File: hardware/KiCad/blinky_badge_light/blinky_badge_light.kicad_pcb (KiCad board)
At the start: 4 copper layers, 108.6 x 87.7 mm, 121 parts, among them Q1 N-Channel MOSFET, Q2 Q_PMOS_GSD, Q3 N-Channel MOSFET, SW1 TS-1187A-B-A-B, U1 ESP32-S3-WROOM-1, U2 TP4056, U3 AP2112K-3.3, U4 MT3608, U5 CP2102N-Axx-xQFN24, U6 SN74LVC1T45DBV

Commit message: change reverse battery protection circuit so diode goes to ground
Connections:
- D28 pad 1: BAT- -> BAT+
- Q1 pad 1: BAT- -> BAT+
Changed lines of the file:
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@@
 			(layers "B.Cu" "B.Mask" "B.Paste")
 			(roundrect_rratio 0.25)
-			(net 59 "BAT-")
+			(net 1 "BAT+")
 			(pinfunction "K")
 			(pintype "passive")
@@
 			(size 1.25 0.7)
 			(layers "B.Cu" "B.Mask" "B.Paste")
-			(net 59 "BAT-")
+			(net 1 "BAT+")
 			(pinfunction "G")
 			(pintype "input")

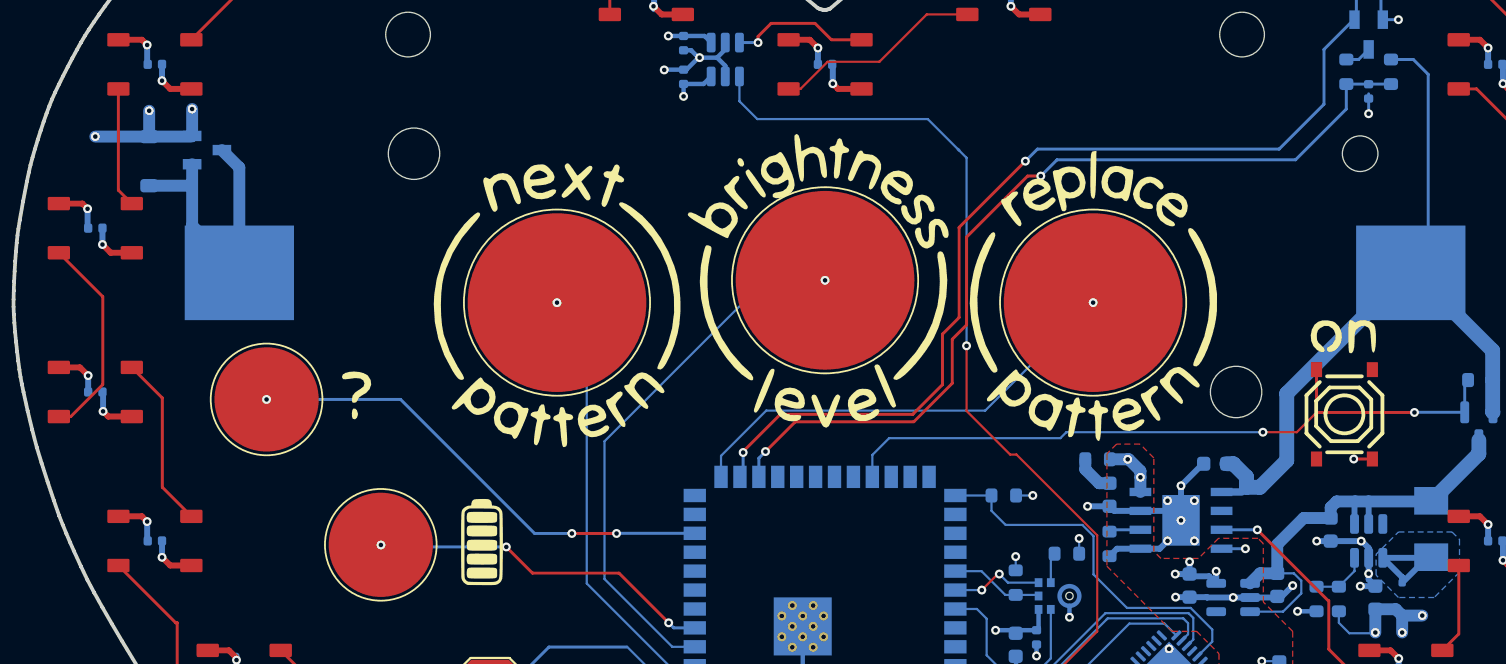
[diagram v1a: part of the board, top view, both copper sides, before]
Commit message: update battery protection circuit and draw routes
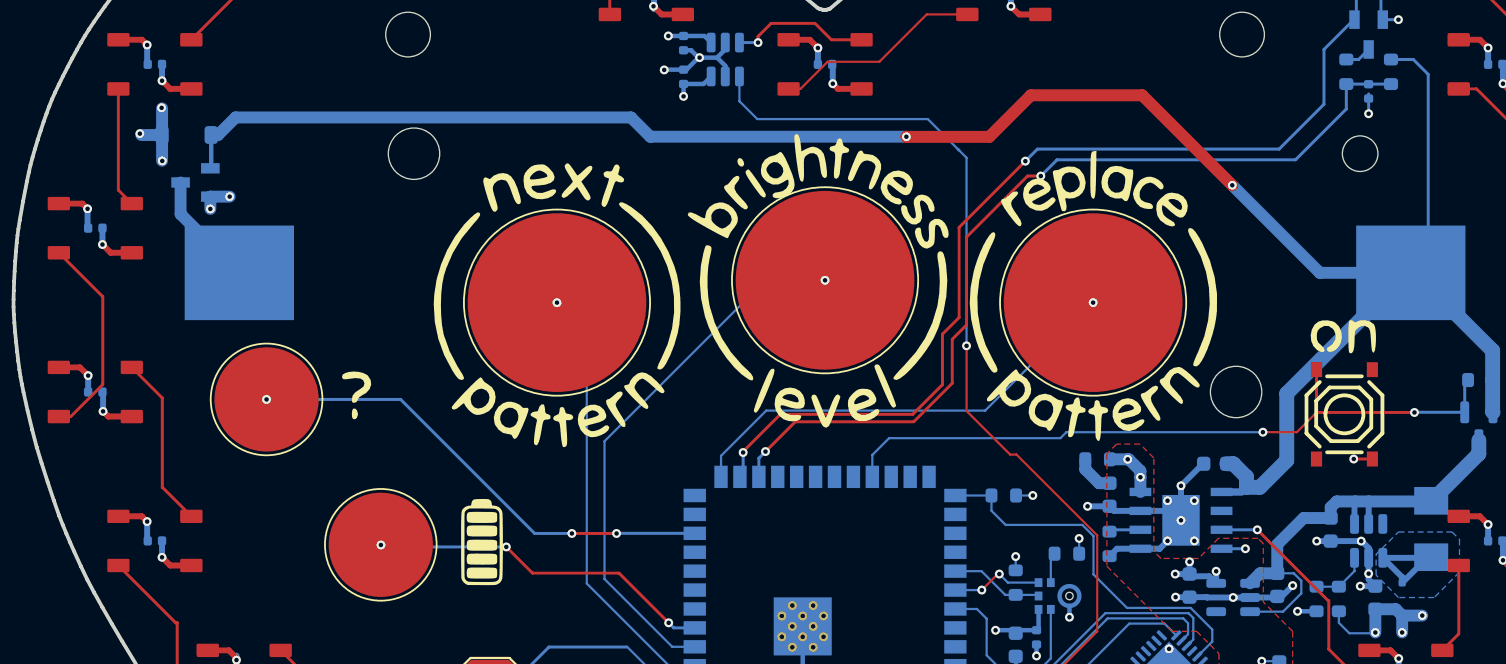
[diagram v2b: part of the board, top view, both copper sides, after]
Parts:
- R13, R18, R19: value 100kΩ -> 10kΩ
- moved D28 3.07 mm to (107.1, 71.7), turned to 180 degrees
- moved Q1 2.31 mm to (107.7, 74.9), turned to 0 degrees
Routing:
- net BAT+: track 52.0 -> 141.9 mm, vias 0 -> 2
- net BAT-: track 20.1 -> 7.70 mm
- net GND: track 179.1 -> 176.3 mm, vias 68 -> 70
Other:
- board text removed: "Battery Monitoring Circuit"
- board text removed: "Q1: is the thickness of the route from R13 to BAT+ ok or should it be thicker?"
- board text removed: "Q2: should these two grounds be the same since they're adjacent?"
- board text removed: "Q3: is it ok that the battery monitoring circuit is so far away from the ESP32?"
- board text removed: "Q4: originally BAT- had a lot of thick connections to GND. Is what I have done here enough?"
- board text removed: "Q5: this routing from battery monitoring to ESP32 is messy but not sure how to improve it.. had to do cross-over also.. open to suggestions"
- board text removed: "Q6: when I do a crossover in routing is it better to make it longer or shorter (did both types here..)"
- board text removed: "Q7a: is this pad too close to BAT -"
- board text removed: "Q7b: is this pad too close to these assorted components?"
- board text removed: "Q8: are the pads supposed to have exposed metal like the boards I got? (I'm just using the detault footprint..)"
- board text removed: "Reverse Polarity Protection"

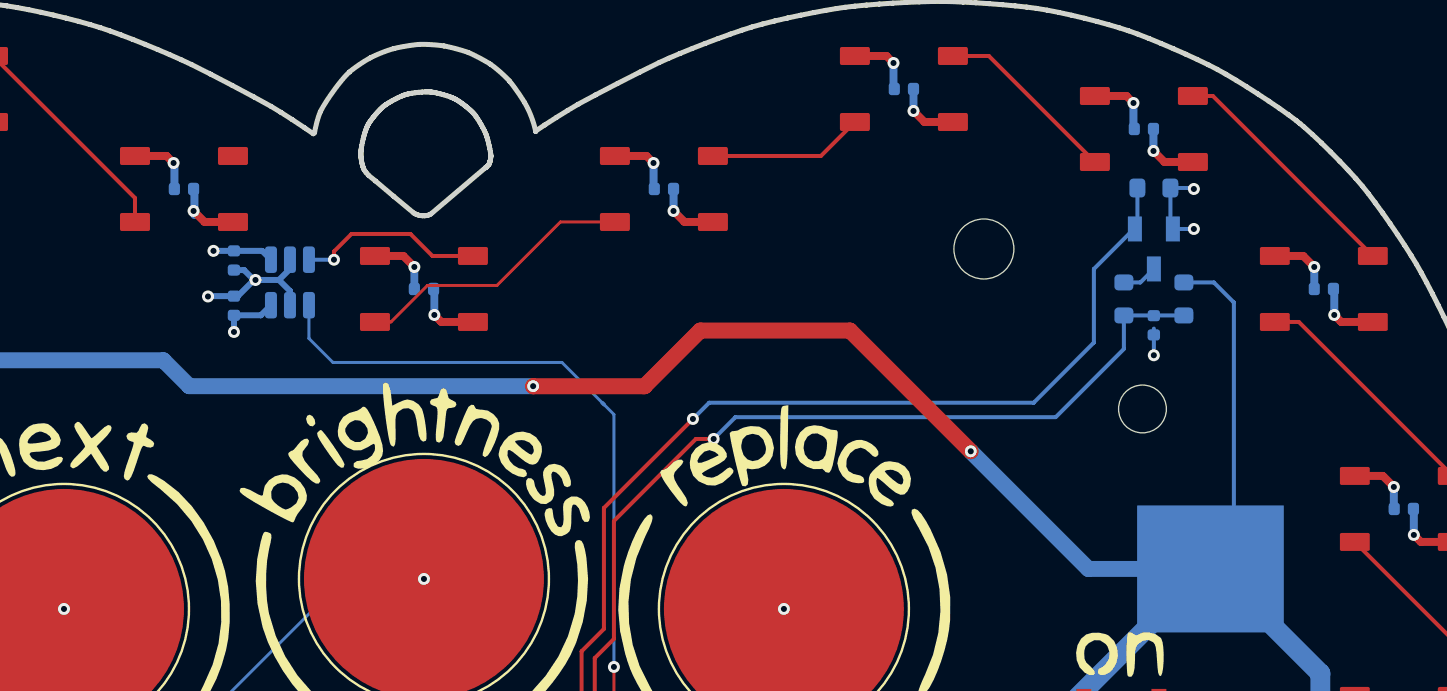
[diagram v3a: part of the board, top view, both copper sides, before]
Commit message: added new transistor and resistor to battery monitoring circuit, adjusted two leds/capacitors position slightly
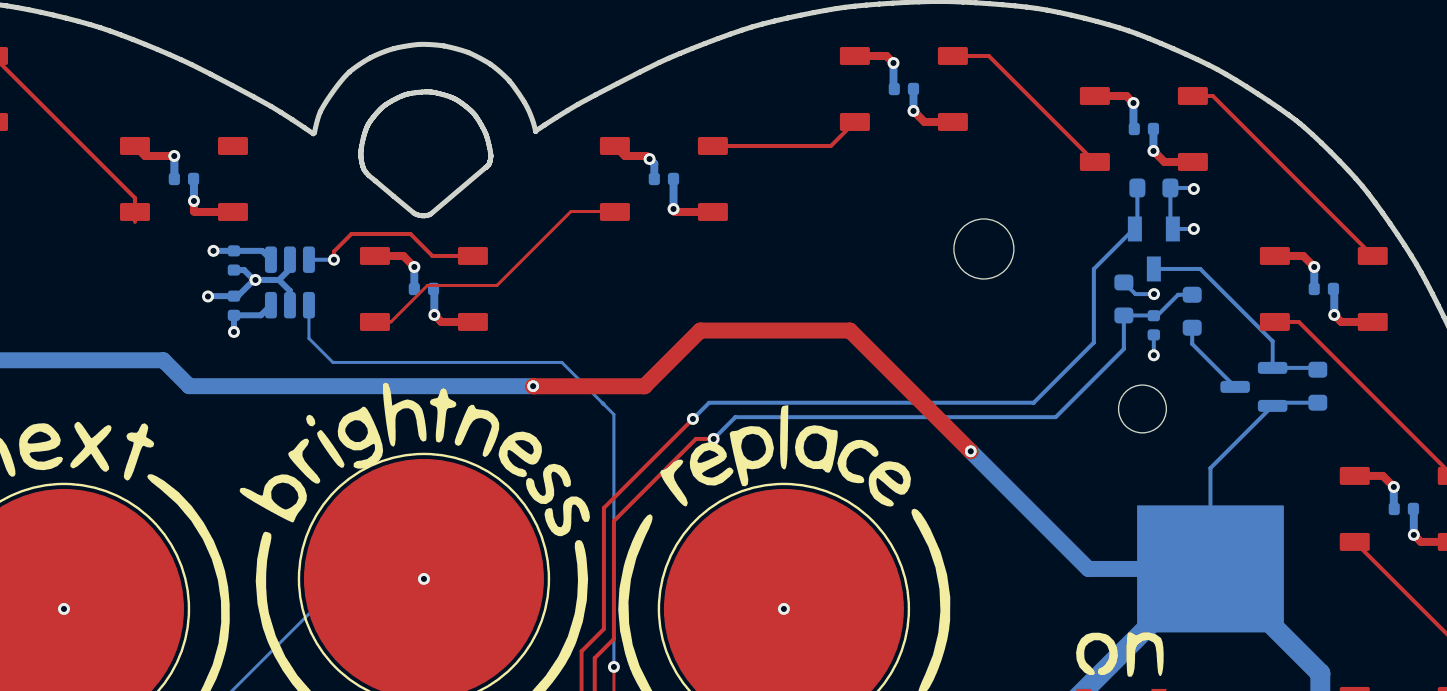
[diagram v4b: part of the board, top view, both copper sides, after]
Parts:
- added Q4: Q_PMOS_GSD, Package_TO_SOT_SMD:SOT-23, B.Cu at (191.5, 71.9)
- added R20: 100kΩ, Resistor_SMD:R_0603_1608Metric, B.Cu at (194.7, 71.9)
- R13, R18, R19: value 10kΩ -> 100kΩ
- moved G*** 4.80 mm to (124.0, 82.7)
- moved G*** 4.57 mm to (175.6, 82.1)
- moved R13 0.74 mm to (188.4, 68.1), turned to -90 degrees
- moved C2 0.50 mm to (162.0, 61.5)
- moved C24 0.50 mm to (138.0, 61.5)
- moved D2 0.50 mm to (162.0, 61.5)
- moved D24 0.50 mm to (138.0, 61.5)
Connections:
- R13 pad 2: BAT+ -> Net-(Q4-D)
- R18 pad 2: Net-(Q3-D) -> GND
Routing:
- net Net-(Q3-D): track 1.78 -> 11.1 mm
- net BAT+: track 141.9 -> 137.0 mm
- net Net-(Q4-D): track 0.00 -> 3.85 mm
- net GND: track 176.3 -> 177.9 mm, vias 70 -> 71
- net ESP32 Battery Monitoring: track 60.3 -> 61.1 mm

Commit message: changed resistors on battery monitoring (back) to 10k
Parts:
- R13, R18, R19, R20: value 100kΩ -> 10kΩ
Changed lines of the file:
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@@
 			)
 		)
-		(property "Value" "100kΩ"
+		(property "Value" "10kΩ"
 			(at 0 -1.43 90)
 			(layer "B.Fab")
@@
 			)
 		)
-		(property "Datasheet" "https://jlcpcb.com/api/file/downloadByFileSystemAccessId/8579706350726930432"
+		(property "Datasheet" "https://jlcpcb.com/api/file/downloadByFileSystemAccessId/8579706381320323072"
 			(at 0 0 270)
 			(unlocked yes)
@@
 			)
 		)
-		(property "JLCPCB Part #" "C25803"
+		(property "JLCPCB Part #" "C25804"
 			(at 0 0 270)
 			(unlocked yes)
@@
 			)
 		)
-		(property "Value" "100kΩ"
+		(property "Value" "10kΩ"
 			(at 0 -1.43 90)
 			(layer "B.Fab")
@@
 			)
 		)
-		(property "Datasheet" "https://jlcpcb.com/api/file/downloadByFileSystemAccessId/8579706350726930432"
+		(property "Datasheet" "https://jlcpcb.com/api/file/downloadByFileSystemAccessId/8579706381320323072"
 			(at 0 0 270)
 			(unlocked yes)
@@
 			)
 		)
-		(property "JLCPCB Part #" "C25803"
+		(property "JLCPCB Part #" "C25804"
 			(at 0 0 270)
 			(unlocked yes)
@@
 			)
 		)
-		(property "Value" "100kΩ"
+		(property "Value" "10kΩ"
 			(at 0 -1.43 0)
 			(layer "B.Fab")
@@
 			)
 		)
-		(property "Datasheet" "https://jlcpcb.com/api/file/downloadByFileSystemAccessId/8579706350726930432"
+		(property "Datasheet" "https://jlcpcb.com/api/file/downloadByFileSystemAccessId/8579706381320323072"
 			(at 0 0 0)
 			(unlocked yes)
@@
 			)
 		)
-		(property "JLCPCB Part #" "C25803"
+		(property "JLCPCB Part #" "C25804"
 			(at 0 0 0)
 			(unlocked yes)
@@
 			)
 		)
-		(property "Value" "100kΩ"
+		(property "Value" "10kΩ"
 			(at 0 -1.43 90)
 			(layer "B.Fab")
@@
 			)
 		)
-		(property "Datasheet" "https://jlcpcb.com/api/file/downloadByFileSystemAccessId/8579706350726930432"
+		(property "Datasheet" "https://jlcpcb.com/api/file/downloadByFileSystemAccessId/8579706381320323072"
 			(at 0 0 90)
 			(unlocked yes)
@@
 			)
 		)
-		(property "JLCPCB Part #" "C25803"
+		(property "JLCPCB Part #" "C25804"
 			(at 0 0 90)
 			(unlocked yes)

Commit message: change charging prog resistor to 2k to keep things cooler
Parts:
- R4: value 1.2kΩ -> 2kΩ
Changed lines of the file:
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@@
 			)
 		)
-		(property "Value" "1.2kΩ"
+		(property "Value" "2kΩ"
 			(at 0 -1.43 90)
 			(layer "B.Fab")
@@
 			)
 		)
-		(property "Datasheet" "https://jlcpcb.com/api/file/downloadByFileSystemAccessId/8579706389601501184"
+		(property "Datasheet" "https://jlcpcb.com/api/file/downloadByFileSystemAccessId/8579706189568917504"
 			(at 0 0 90)
 			(unlocked yes)
@@
 			)
 		)
-		(property "JLCPCB Part #" "C22764"
+		(property "JLCPCB Part #" "C22975"
 			(at 0 0 270)
 			(unlocked yes)

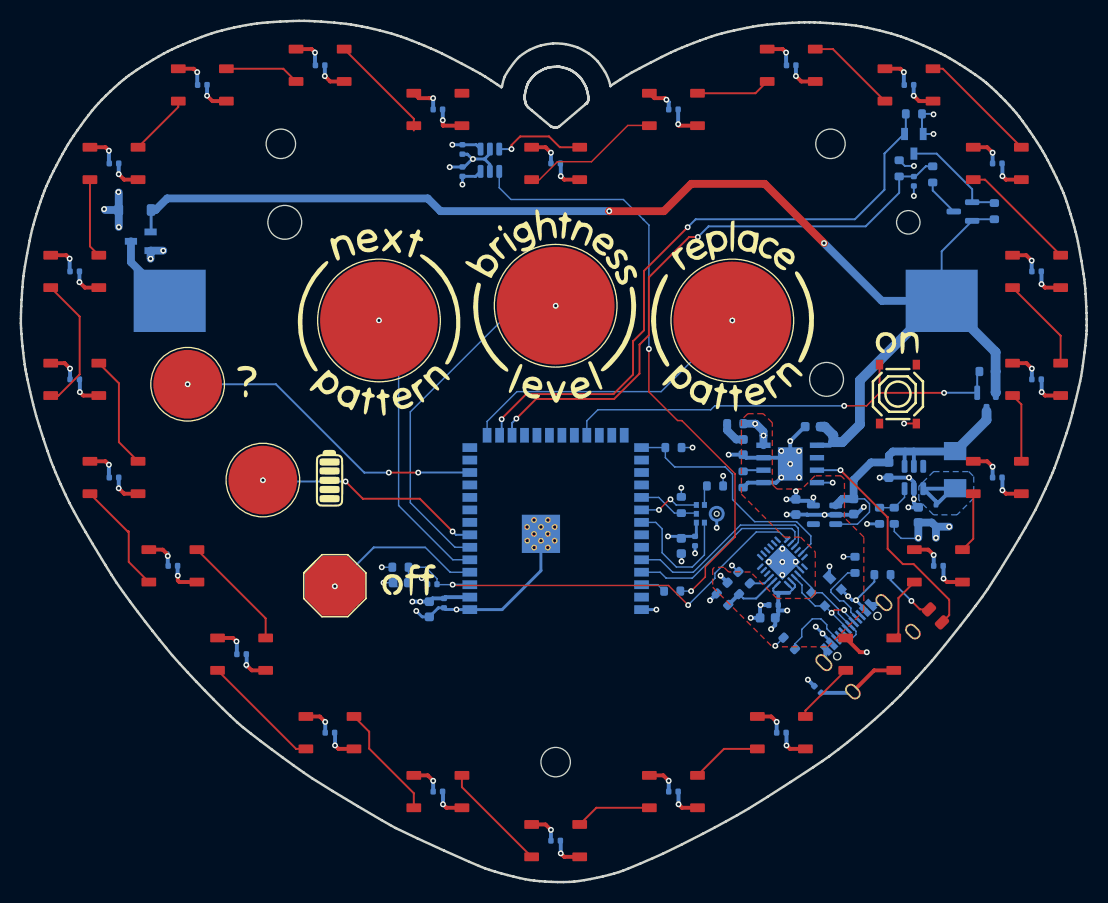
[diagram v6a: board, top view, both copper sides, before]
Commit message: slight adjusting of led positions to make things fit more nicely under the front cover
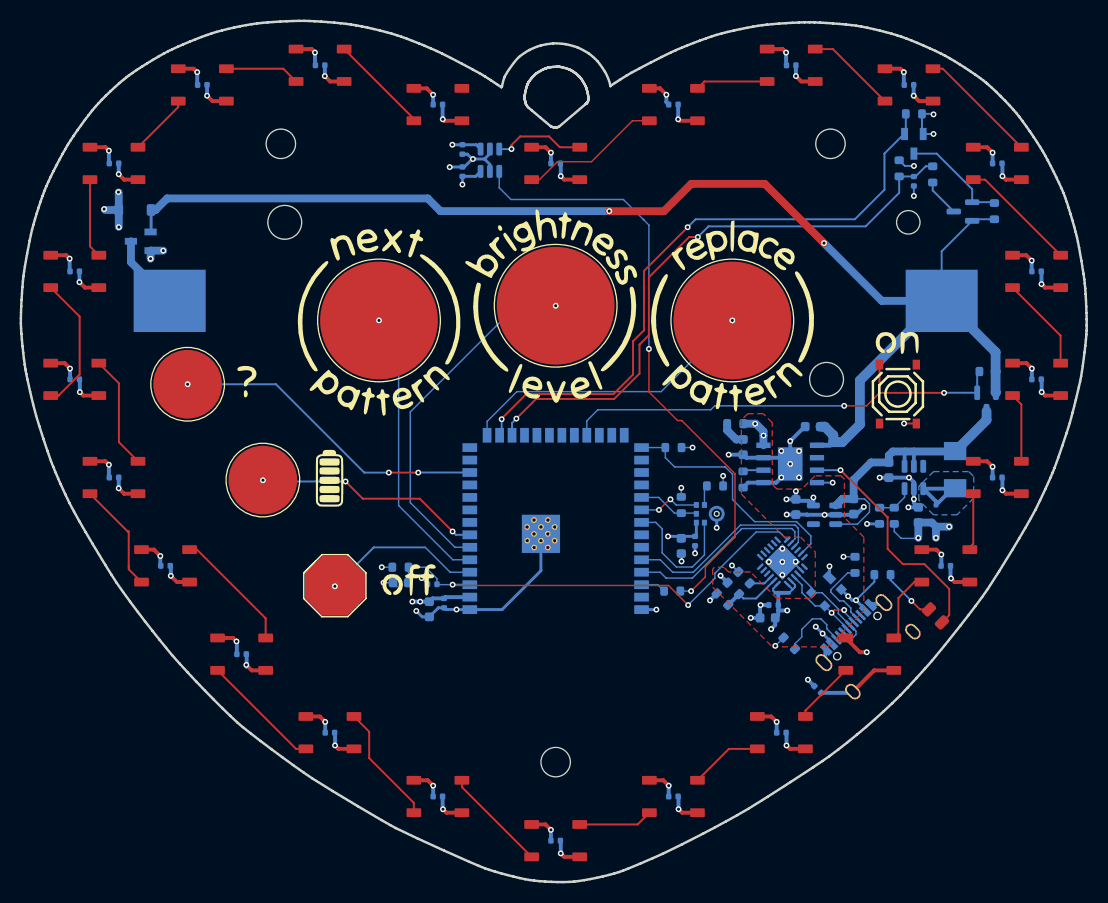
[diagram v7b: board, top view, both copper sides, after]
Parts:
- moved C17 0.75 mm to (110.2, 108.0)
- moved C9 0.75 mm to (189.8, 108.0)
- moved D17 0.75 mm to (110.2, 108.0)
- moved D9 0.75 mm to (189.8, 108.0)
- moved C12 0.50 mm to (162.0, 131.5)
- moved C14 0.50 mm to (138.0, 131.5)
- moved C2 0.50 mm to (162.0, 61.0)
- moved C24 0.50 mm to (138.0, 61.0)
- moved D12 0.50 mm to (162.0, 131.5)
- moved D14 0.50 mm to (138.0, 131.5)
- moved D2 0.50 mm to (162.0, 61.0)
- moved D24 0.50 mm to (138.0, 61.0)
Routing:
- net Net-(D16-DOUT): track 11.9 -> 12.6 mm
- net Net-(D10-DIN): track 6.57 -> 7.32 mm
- net Net-(D23-DOUT): track 11.2 -> 10.5 mm
- net Net-(D25-K): track 23.5 -> 24.1 mm
- net GND: track 177.9 -> 177.4 mm
- net Net-(D13-DOUT): track 11.2 -> 10.7 mm
